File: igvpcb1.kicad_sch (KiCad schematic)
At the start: 19 parts

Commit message: all submodules added
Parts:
- removed C? (x3): 10u, Capacitor_SMD:C_0603_1608Metric_Pad1.08x0.95mm_HandSolder, symbol Device:C
- removed C? (x2): 22pF, Capacitor_SMD:C_0603_1608Metric_Pad1.08x0.95mm_HandSolder, symbol Device:C_Small
- removed C? (x4): 100n, Capacitor_SMD:C_0603_1608Metric_Pad1.08x0.95mm_HandSolder, symbol Device:C
- removed C?: 1u, Capacitor_SMD:C_0603_1608Metric_Pad1.08x0.95mm_HandSolder, symbol Device:C
- removed C?: 10n, Capacitor_SMD:C_0603_1608Metric_Pad1.08x0.95mm_HandSolder, symbol Device:C
- removed R?: 10Meg, Resistor_SMD:R_0805_2012Metric_Pad1.20x1.40mm_HandSolder, symbol Device:R_US
- removed U?: LSM9DS1, Package_LGA:LGA-24L_3x3.5mm_P0.43mm, symbol Sensor_Motion:LSM9DS1
- removed U?: RXM-GPS-RM, RF_GPS:Linx_RXM-GPS, symbol RF_GPS:RXM-GPS-RM
- removed U?: IFX27001TFV33, Package_TO_SOT_SMD:TO-252-3_TabPin2, symbol Regulator_Linear:IFX27001TFV33
- removed Y?: 16MHz, symbol Device:Crystal
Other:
- added sheet Battery Charger (battery_charger.kicad_sch)
- added sheet Circuit Protections(SC, Reverse Polarity, Overvoltage, Inrush current) (circuit_protection.kicad_sch)
- added sheet Motor Controller (motor_controller.kicad_sch)
- added sheet Sensors (sensors.kicad_sch)
- note added: "Motor Controllers"
- note removed: "External Clock"
- note removed: "LDO 5V to 3.3V"
- note removed: "Low pass filter"
- note removed: "Sensors"
- note removed: "Sensors Bypass Caps"
- moved on the sheet: D?, J?

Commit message: added hierarchical labels
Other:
- sheet Battery Charger ports: added GND, Vcc, Vout; removed none
- sheet Circuit Protections(SC, Reverse Polarity, Overvoltage, Inrush current) ports: added GND, Vin, Vout; removed none
- sheet MCU_main ports: added GND, RX, SCL, SDA, TX, Vcc; removed none
- sheet Sensors ports: added GND, SCL, SDA, Vcc; removed none
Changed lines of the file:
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@@
       (effects (font (size 1.27 1.27)) (justify left top))
+    )
+    (pin "GND" input (at 326.39 241.3 270)
+      (effects (font (size 1.27 1.27)) (justify left))
+    )
+    (pin "Vout" input (at 388.62 160.02 0)
+      (effects (font (size 1.27 1.27)) (justify right))
+    )
+    (pin "Vcc" input (at 259.08 160.02 180)
+      (effects (font (size 1.27 1.27)) (justify left))
     )
   )
@@
       (effects (font (size 1.27 1.27)) (justify left top))
     )
+    (pin "Vout" input (at 388.62 83.82 0)
+      (effects (font (size 1.27 1.27)) (justify right))
+    )
+    (pin "Vin" input (at 304.8 83.82 180)
+      (effects (font (size 1.27 1.27)) (justify left))
+    )
+    (pin "GND" input (at 346.71 129.54 270)
+      (effects (font (size 1.27 1.27)) (justify left))
+    )
   )
   (sheet (at 34.29 33.02) (size 82.55 128.27) (fields_autoplaced)
@@
     (property "Sheet file" "mcu_main.kicad_sch" (id 1) (at 34.29 161.8746 0)
       (effects (font (size 1.27 1.27)) (justify left top))
+    )
+    (pin "GND" input (at 69.85 161.29 270)
+      (effects (font (size 1.27 1.27)) (justify left))
+    )
+    (pin "RX" input (at 116.84 106.68 0)
+      (effects (font (size 1.27 1.27)) (justify right))
+    )
+    (pin "TX" input (at 116.84 113.03 0)
+      (effects (font (size 1.27 1.27)) (justify right))
+    )
+    (pin "SDA" input (at 116.84 132.08 0)
+      (effects (font (size 1.27 1.27)) (justify right))
+    )
+    (pin "SCL" input (at 116.84 137.16 0)
+      (effects (font (size 1.27 1.27)) (justify right))
+    )
+    (pin "Vcc" input (at 34.29 64.77 180)
+      (effects (font (size 1.27 1.27)) (justify left))
     )
   )
@@
       (effects (font (size 1.27 1.27)) (justify left top))
     )
+    (pin "SCL" input (at 200.66 95.25 180)
+      (effects (font (size 1.27 1.27)) (justify left))
+    )
+    (pin "SDA" input (at 200.66 100.33 180)
+      (effects (font (size 1.27 1.27)) (justify left))
+    )
+    (pin "Vcc" input (at 243.84 50.8 90)
+      (effects (font (size 1.27 1.27)) (justify right))
+    )
+    (pin "GND" input (at 243.84 129.54 270)
+      (effects (font (size 1.27 1.27)) (justify left))
+    )
   )
   (sheet_instances
@@
       (reference "#PWR?") (unit 1) (value "+5V") (footprint "")
     )
-    (path "/5417062a-2c0a-4eb1-a915-06a0ec20ee38/36fd5727-f35c-4116-b850-e44d05e3f6bf"
-      (reference "#PWR?") (unit 1) (value "+3.3V") (footprint "")
-    )
     (path "/16d6dd37-0750-413d-a336-fa0a8946c270/3ac7ddd8-cfca-4be5-995a-094cc6cd12f5"

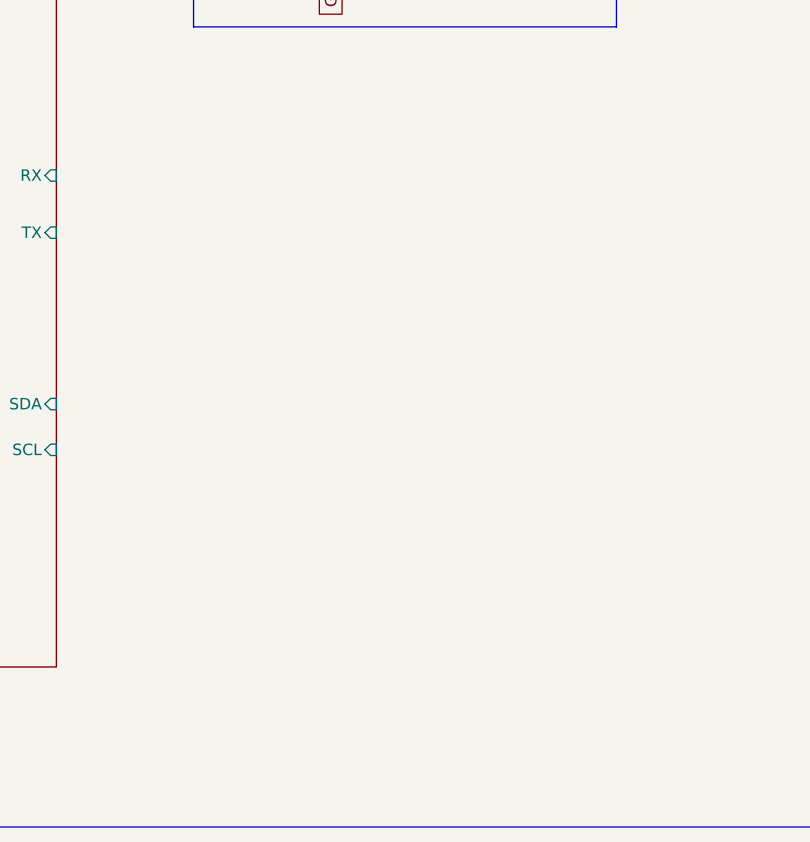
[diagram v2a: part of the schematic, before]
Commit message: added symbols for battery charger module
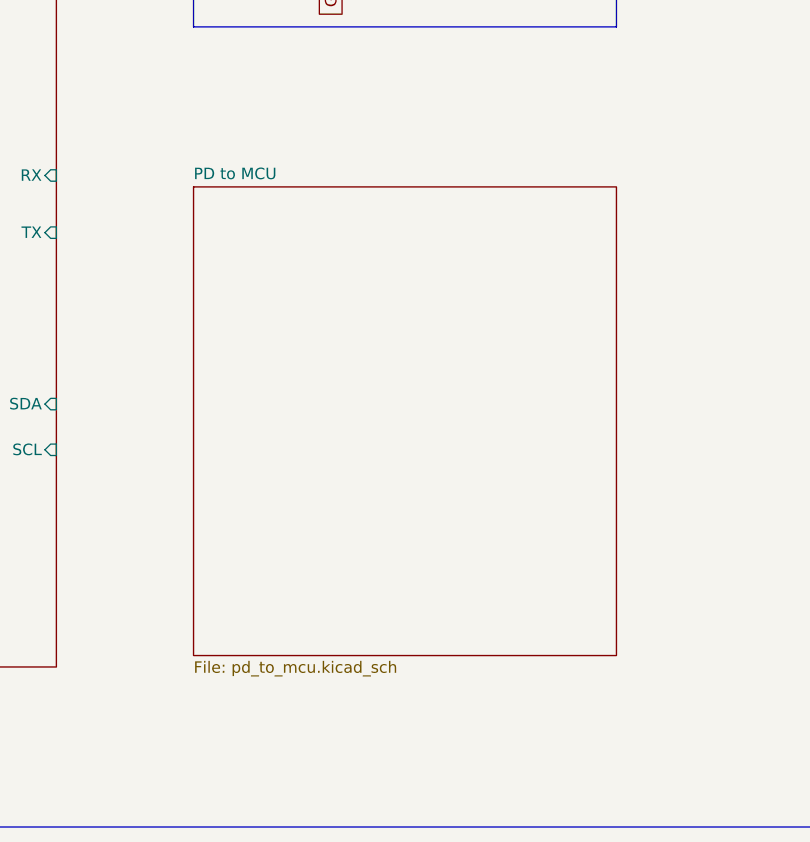
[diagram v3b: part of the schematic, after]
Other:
- added sheet PD to MCU (pd_to_mcu.kicad_sch)
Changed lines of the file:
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@@
+    )
+  )
+  (sheet (at 132.08 107.95) (size 46.99 52.07) (fields_autoplaced)
+    (stroke (width 0.1524) (type solid) (color 0 0 0 0))
+    (fill (color 0 0 0 0.0000))
+    (property "Sheet name" "PD to MCU" (id 0) (at 132.08 107.2384 0)
+      (effects (font (size 1.27 1.27)) (justify left bottom))
+    )
+    (property "Sheet file" "pd_to_mcu.kicad_sch" (id 1) (at 132.08 160.6046 0)
+      (effects (font (size 1.27 1.27)) (justify left top))
     )
   )
@@
     (path "/f05ee547-e32d-4987-a40e-18e5437d043b" (page "5"))
     (path "/328398a8-3e10-4a92-962c-9ac39a57a765" (page "6"))
+    (path "/e7e79c7b-92f9-4117-9d4e-88e251ee87d9" (page "7"))
   )
   (symbol_instances
@@
       (reference "J?") (unit 1) (value "USB_C_Receptacle_USB2.0") (footprint "")
     )
+    (path "/328398a8-3e10-4a92-962c-9ac39a57a765/0044b924-bce2-40ae-967d-8f83545bb550"
+      (reference "Q?") (unit 1) (value "SIR186LDP-T1-RE3") (footprint "SamacSys_Parts:SI7141DPT1GE3")
+    )
+    (path "/328398a8-3e10-4a92-962c-9ac39a57a765/03760f51-7700-4488-ba94-50fc4ed6fd2f"
+      (reference "Q?") (unit 1) (value "SIR186LDP-T1-RE3") (footprint "SamacSys_Parts:SI7141DPT1GE3")
+    )
+    (path "/328398a8-3e10-4a92-962c-9ac39a57a765/6b3aa70e-1e2a-44c9-a526-bab4768cc418"
+      (reference "Q?") (unit 1) (value "SIR186LDP-T1-RE3") (footprint "SamacSys_Parts:SI7141DPT1GE3")
+    )
+    (path "/328398a8-3e10-4a92-962c-9ac39a57a765/c1db2469-617c-4f5a-992e-8c67c51120dc"
+      (reference "Q?") (unit 1) (value "SIR186LDP-T1-RE3") (footprint "SamacSys_Parts:SI7141DPT1GE3")
+    )
+    (path "/328398a8-3e10-4a92-962c-9ac39a57a765/f66299b9-283b-4455-80cd-d4bff1576929"
+      (reference "Q?") (unit 1) (value "SIR165DP-T1-GE3") (footprint "SamacSys_Parts:SI7141DPT1GE3")
+    )
     (path "/16d6dd37-0750-413d-a336-fa0a8946c270/30fdc93c-38b6-4132-99cc-7d0c0f46f28f"
       (reference "R?") (unit 1) (value "10k") (footprint "Resistor_SMD:R_0805_2012Metric_Pad1.20x1.40mm_HandSolder")
@@
       (reference "SW?") (unit 1) (value "SW_Push") (footprint "")
     )
+    (path "/328398a8-3e10-4a92-962c-9ac39a57a765/43a6c8f5-dd50-40be-957c-a7c1fa16368a"
+      (reference "U?") (unit 1) (value "BQ25720") (footprint "userdef:QFN-32_EP_4x4_Pitch0.4mm")
+    )
     (path "/16d6dd37-0750-413d-a336-fa0a8946c270/4b61f4d4-6d8b-4d04-954d-313be85f0769"

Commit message: updated UPD module
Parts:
- removed D? (x2): D_TVS, Diode_SMD:D_1206_3216Metric_Pad1.42x1.75mm_HandSolder, symbol Device:D_TVS
- removed J?: USB_C_Receptacle_USB2.0, symbol Connector:USB_C_Receptacle_USB2.0
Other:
- sheet MCU_main ports: added MISO, MOSI, SCK, ~{SS}; removed none
- note removed: "USB"

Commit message: updated for winter 2022
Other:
- sheet MCU_main ports: added D+, D-, INT0, INT1, INT2, INT3, INT4, INT5, INT6, INT7; removed MISO, MOSI, SCK, ~{SS}
- sheet PD to MCU ports: added CC1, CC2, D+, D-, I2C_CLK_3V3, I2C_DAT_3V3, VBUS, VBUS_DET, VCONN, VSW, ~{PD_IRQ}, ~{PD_RESET}; removed none
